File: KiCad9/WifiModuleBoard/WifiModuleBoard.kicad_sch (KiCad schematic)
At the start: 10 parts, among them J2 Conn_01x07_Pin, J3 TC2030, J4 Conn_01x05_Pin, U1 ESP32-C5-WROOM-1U-N8R8

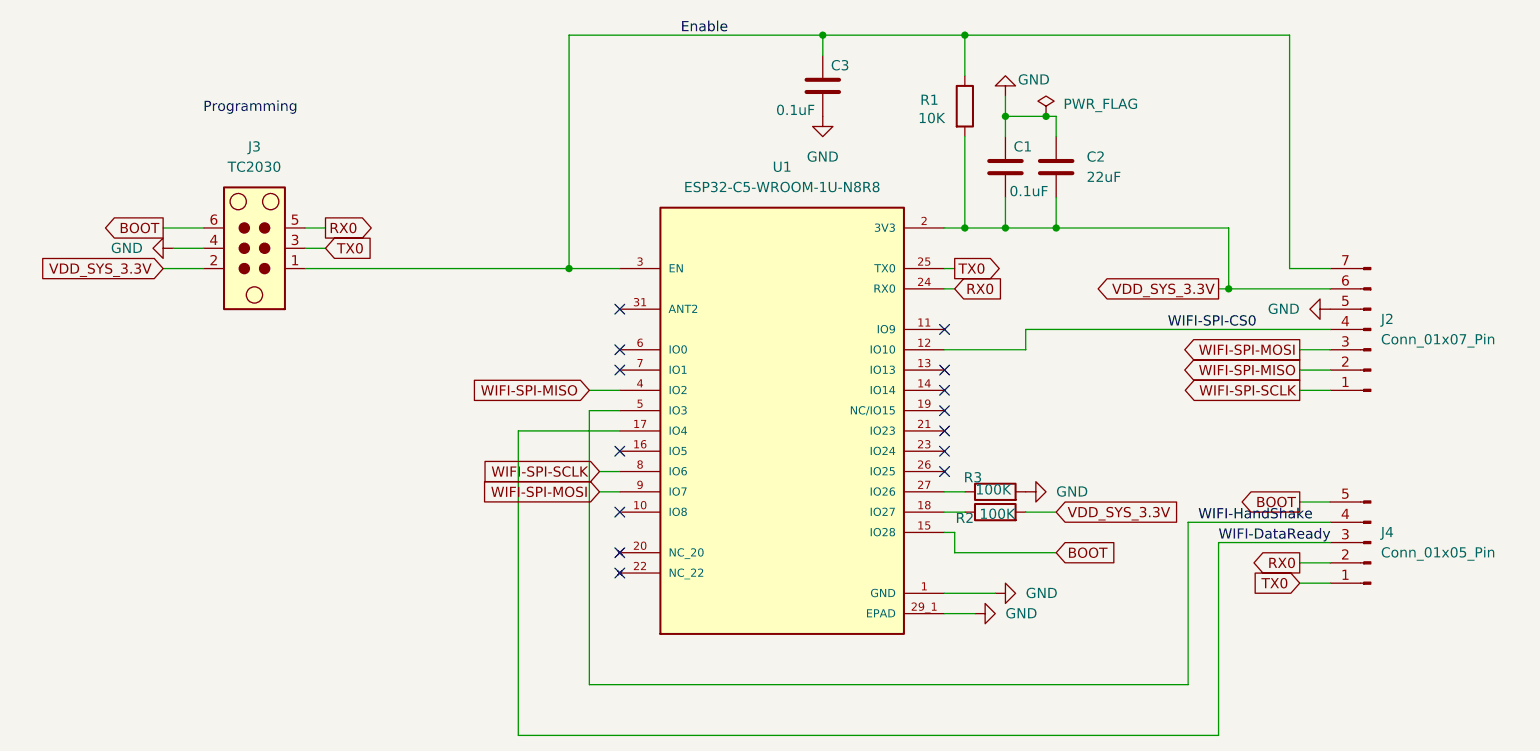
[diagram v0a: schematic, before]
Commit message: add 3d of wifiboard
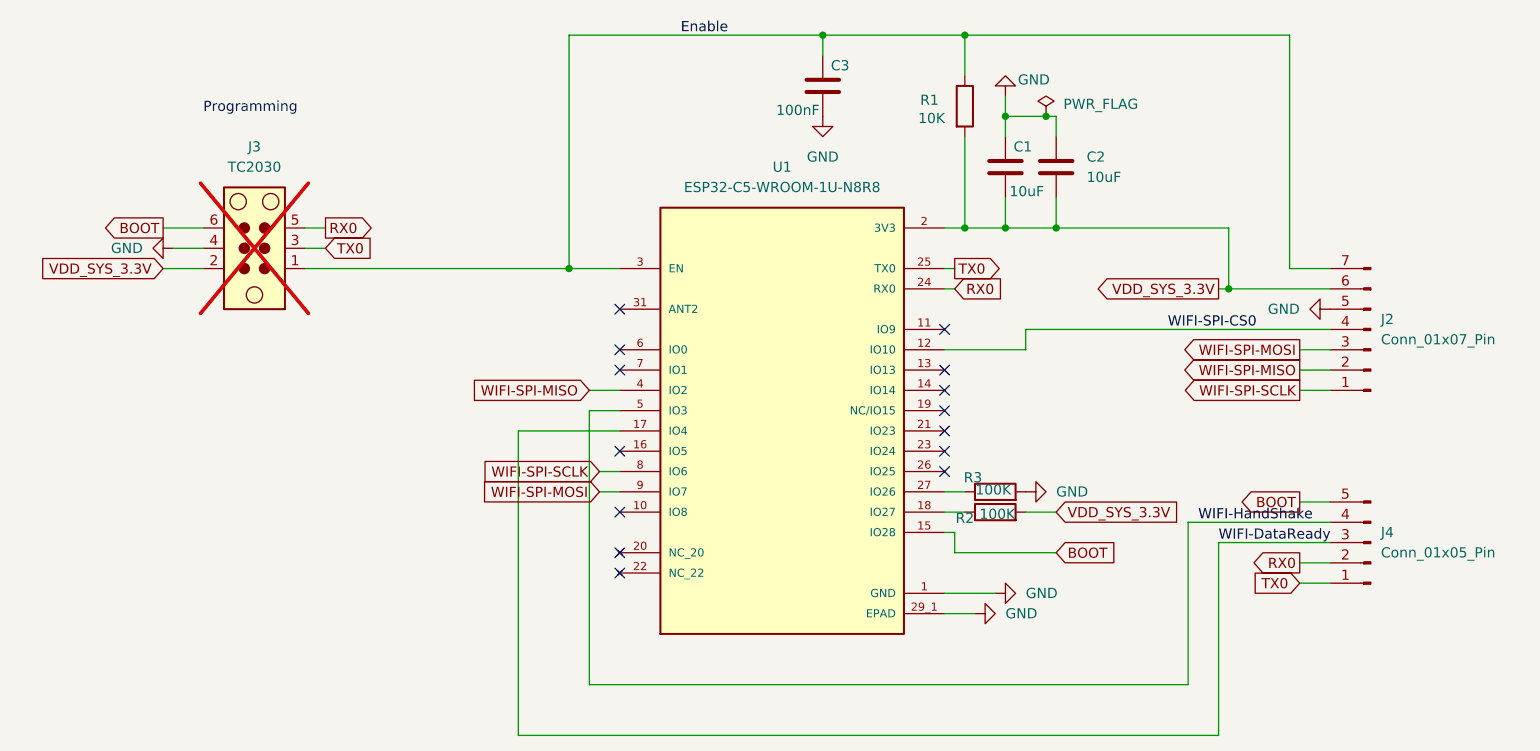
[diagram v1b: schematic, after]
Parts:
- C1: value 0.1uF -> 10uF; LCSC Part# (none) -> C15525; Manufacturer (none) -> Samsung Electro-Mechanics; ManufacturerPartNumber (none) -> CL05A106MQ5NUNC
- C2: value 22uF -> 10uF; LCSC Part# (none) -> C15525; Manufacturer (none) -> Samsung Electro-Mechanics; ManufacturerPartNumber (none) -> CL05A106MQ5NUNC
- C3: value 0.1uF -> 100nF; LCSC Part# (none) -> C1525; Manufacturer (none) -> Samsung Electro-Mechanics; ManufacturerPartNumber (none) -> CL05B104KO5NNNC
- J2: footprint Connector_PinHeader_1.27mm:PinHeader_1x07_P1.27mm_Vertical_SMD_Pin1Left -> Connector_PinSocket_1.27mm:PinSocket_1x07_P1.27mm_Vertical_SMD_Pin1Left
- J3: now not fitted
- J4: footprint Connector_PinHeader_1.27mm:PinHeader_1x05_P1.27mm_Vertical_SMD_Pin1Left -> Connector_PinSocket_1.27mm:PinSocket_1x05_P1.27mm_Vertical_SMD_Pin1Left
- R1: LCSC Part# (none) -> C25744; Manufacturer (none) -> Uniroyal Elec; ManufacturerPartNumber (none) -> 0402WGF1002TCE
- R2, R3: LCSC Part# (none) -> C25741; Manufacturer (none) -> Uniroyal Elec; ManufacturerPartNumber (none) -> 0402WGF1003TCE
